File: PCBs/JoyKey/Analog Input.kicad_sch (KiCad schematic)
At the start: 2 parts, among them SW1 RotaryEncoder_Switch, U5 2_axis_analog_joystick_button

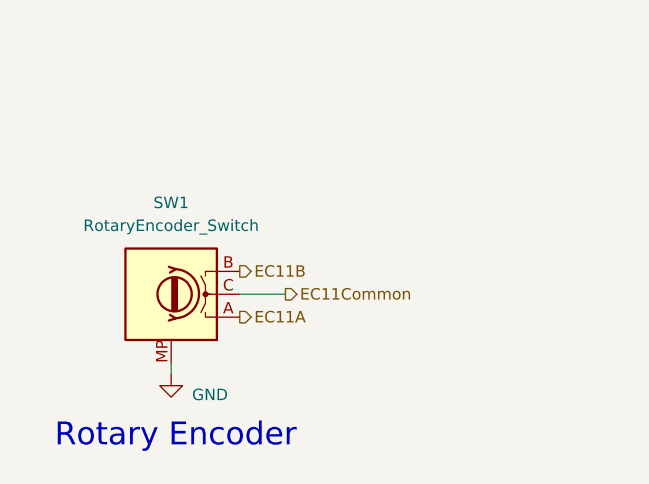
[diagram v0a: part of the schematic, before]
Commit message: Switched encoder to Alps SRBE110301 in sch
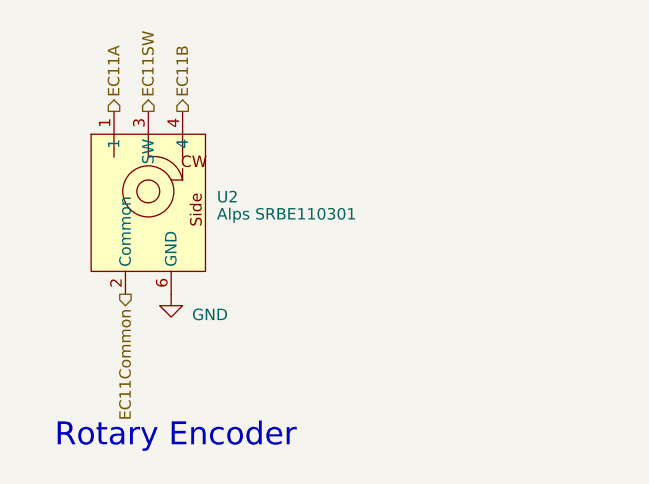
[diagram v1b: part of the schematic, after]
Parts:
- removed SW1: RotaryEncoder_Switch, Rotary_Encoder:RotaryEncoder_Alps_EC12E_Vertical_H20mm, symbol Device:RotaryEncoder
- added U2: Alps SRBE110301, custom_Interface_HID:Alps SRBE110301, symbol custom_Interface_HID:Alps_SRBE110301
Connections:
- net EC11A: now also U2.1
- net EC11B: now also U2.4
- net EC11Common: now also U2.2 (Common)
- net GND: now also U2.5 (GND), U2.6 (GND)
- new net EC11SW: U2.3 (SW)
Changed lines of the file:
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@@
 	(wire
 		(pts
-			(xy 127 87.63) (xy 121.92 87.63)
+			(xy 184.15 72.39) (xy 184.15 80.01)
 		)
 		(stroke
@@
 		)
 	)
-	(wire
-		(pts
-			(xy 184.15 72.39) (xy 184.15 80.01)
-		)
-		(stroke
-			(width 0)
-			(type default)
-		)
-	)
-	(wire
-		(pts
-			(xy 114.3 96.52) (xy 114.3 95.25)
-		)
-		(stroke
-			(width 0)
-			(type default)
-		)
-	)
 	(hierarchical_label "StickButtonB"
 		(shape output)
@@
 	(hierarchical_label "EC11A"
 		(shape output)
-		(at 121.92 90.17 0)
+		(at 107.95 67.31 90)
+		(effects
+			(font
+				(size 1.27 1.27)
+			)
+			(justify left)
+		)
+	)
+	(hierarchical_label "EC11SW"
+		(shape output)
+		(at 111.76 67.31 90)
 		(effects
 			(font
@@
 	(hierarchical_label "EC11B"
 		(shape output)
-		(at 121.92 85.09 0)
+		(at 115.57 67.31 90)
 		(effects
 			(font
@@
 	(hierarchical_label "EC11Common"
 		(shape output)
-		(at 127 87.63 0)
-		(effects
-			(font
-				(size 1.27 1.27)
-			)
-			(justify left)
+		(at 109.22 87.63 270)
+		(effects
+			(font
+				(size 1.27 1.27)
+			)
+			(justify right)
 		)
 	)
@@
 	)
 	(symbol
-		(lib_id "Device:RotaryEncoder")
-		(at 114.3 87.63 180)
+		(lib_id "custom_Interface_HID:Alps_SRBE110301")
+		(at 111.76 76.2 0)
 		(unit 1)
 		(exclude_from_sim no)
@@
 		(dnp no)
 		(fields_autoplaced yes)
-		(property "Reference" "SW1"
-			(at 114.3 77.47 0)
-			(effects
-				(font
-					(size 1.27 1.27)
-				)
-			)
-		)
-		(property "Value" "RotaryEncoder_Switch"
-			(at 114.3 80.01 0)
-			(effects
-				(font
-					(size 1.27 1.27)
-				)
-			)
-		)
-		(property "Footprint" "Rotary_Encoder:RotaryEncoder_Alps_EC12E_Vertical_H20mm"
-			(at 118.11 91.694 0)
-			(effects
-				(font
-					(size 1.27 1.27)
-				)
-				(hide yes)
-			)
-		)
-		(property "Datasheet" "~"
-			(at 114.3 94.234 0)
-			(effects
-				(font
-					(size 1.27 1.27)
-				)
-				(hide yes)
-			)
-		)
-		(property "Description" "Rotary encoder, dual channel, incremental quadrate outputs"
-			(at 114.3 87.63 0)
-			(effects
-				(font
-					(size 1.27 1.27)
-				)
-				(hide yes)
-			)
-		)
-		(pin "A"
-		)
-		(pin "B"
-		)
-		(pin "C"
-		)
-		(pin "MP"
+		(property "Reference" "U2"
+			(at 119.38 76.8349 0)
+			(effects
+				(font
+					(size 1.27 1.27)
+				)
+				(justify left)
+			)
+		)
+		(property "Value" "Alps SRBE110301"
+			(at 119.38 78.74 0)
+			(effects
+				(font
+					(size 1.27 1.27)
+				)
+				(justify left)
+			)
+		)
+		(property "Footprint" "custom_Interface_HID:Alps SRBE110301"
+			(at 111.76 76.2 0)
+			(effects
+				(font
+					(size 1.27 1.27)
+				)
+				(hide yes)
+			)
+		)
+		(property "Datasheet" ""
+			(at 111.76 76.2 0)
+			(effects
+				(font
+					(size 1.27 1.27)
+				)
+				(hide yes)
+			)
+		)
+		(property "Description" ""
+			(at 111.76 76.2 0)
+			(effects
+				(font
+					(size 1.27 1.27)
+				)
+				(hide yes)
+			)
+		)
+		(pin "5"
+		)
+		(pin "3"
+		)
+		(pin "6"
+		)
+		(pin "4"
+		)
+		(pin "2"
+		)
+		(pin "1"
 		)
 		(instances
 			(project "JoyKey"
 				(path "/7995ec7a-c14b-437e-b354-3eb74052b7cb/a78c392f-6f7c-48a6-aa3f-986a350bb68a"
-					(reference "SW1")
+					(reference "U2")
 					(unit 1)
 				)
@@
 	(symbol
 		(lib_id "power:GND")
-		(at 114.3 96.52 0)
+		(at 114.3 87.63 0)
 		(unit 1)
 		(exclude_from_sim no)
@@
 		(dnp no)
 		(property "Reference" "#PWR012"
-			(at 114.3 102.87 0)
+			(at 114.3 93.98 0)
 			(effects
 				(font
@@
 		)
 		(property "Value" "GND"
-			(at 118.618 98.806 0)
+			(at 118.618 89.916 0)
 			(effects
 				(font
@@
 		)
 		(property "Footprint" ""
-			(at 114.3 96.52 0)
-			(effects
-				(font
-					(size 1.27 1.27)
-				)
-				(hide yes)
-			)
-		)
-		(property "Datasheet" ""
-			(at 114.3 96.52 0)
+			(at 114.3 87.63 0)
+			(effects
+				(font
+					(size 1.27 1.27)
+				)
+				(hide yes)
+			)
+		)
+		(property "Datasheet" ""
+			(at 114.3 87.63 0)
 			(effects
 				(font
@@
 		)
 		(property "Description" "Power symbol creates a global label with name \"GND\" , ground"
-			(at 114.3 96.52 0)
-			(effects
-				(font
+			(at 114.3 87.63 0)
+			(effects
+				(font

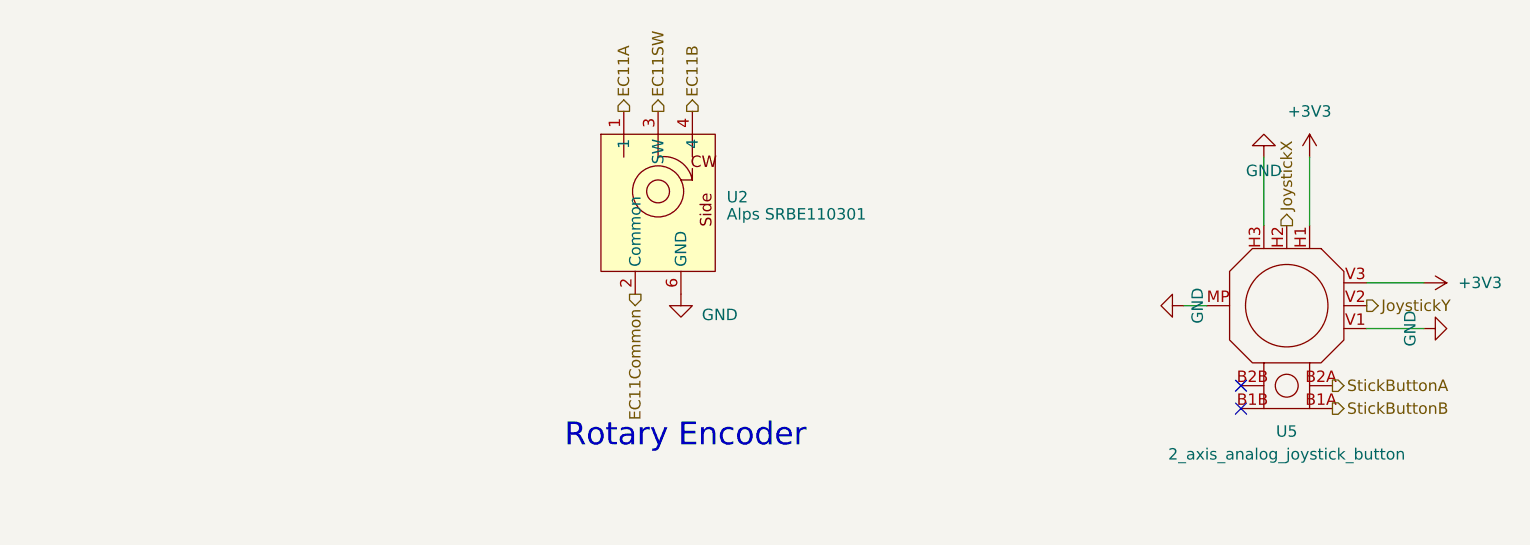
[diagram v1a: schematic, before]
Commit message: Add reverse mount for side encoder to simplifiy assembly
Now, if you want, you can get ALL SMD components on one side! I still prefer the encoder to be put on the top side because it is more central to the whole body, but of course, 2 sided assembly has its costs and I wanted to minimize that.
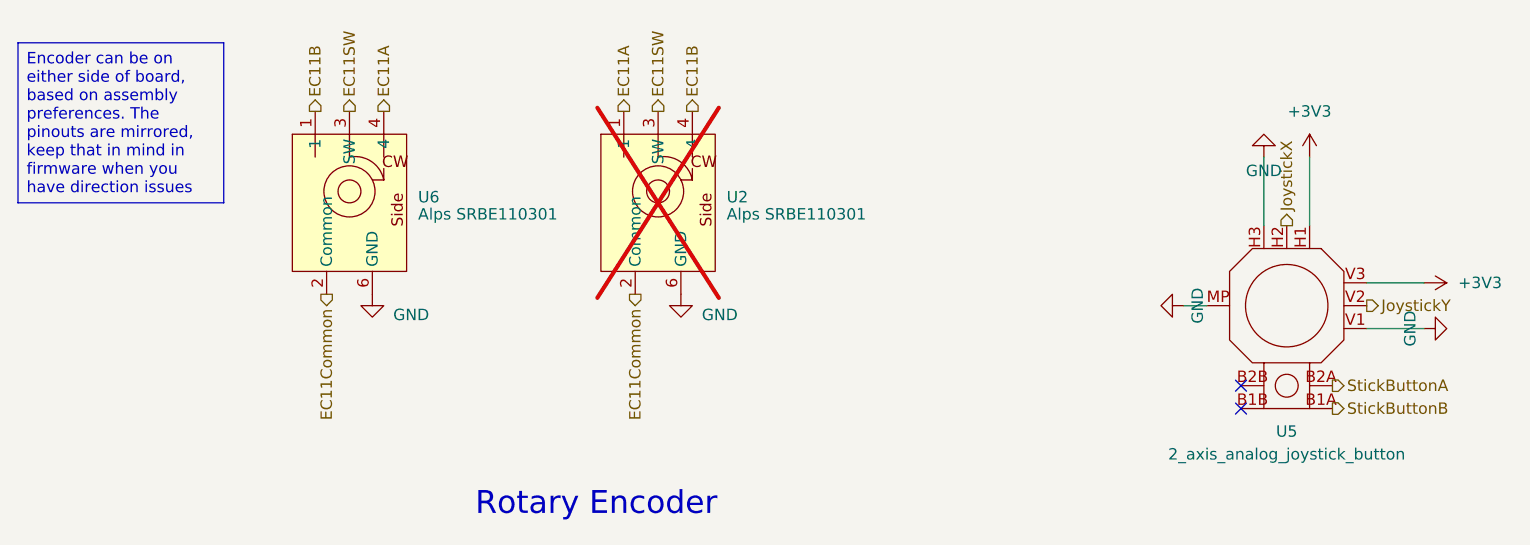
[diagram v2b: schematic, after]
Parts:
- added U6: Alps SRBE110301, custom_Interface_HID:Alps SRBE110301, symbol custom_Interface_HID:Alps_SRBE110301
- U2: now not fitted; now left out of the parts list
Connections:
- net EC11A: now also U6.4
- net EC11B: now also U6.1
- net EC11Common: now also U6.2 (Common)
- net EC11SW: now also U6.3 (SW)
- net GND: now also U6.5 (GND), U6.6 (GND)
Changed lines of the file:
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@@
 	(text "Rotary Encoder"
 		(exclude_from_sim no)
-		(at 114.808 103.378 0)
+		(at 104.902 110.998 0)
 		(effects
 			(font
 				(size 2.54 2.54)
 			)
+		)
+	)
+	(text_box "Encoder can be on either side of board, based on assembly preferences. The pinouts are mirrored, keep that in mind in firmware when you have direction issues"
+		(exclude_from_sim no)
+		(at 40.64 59.69 0)
+		(size 22.86 17.78)
+		(margins 0.9525 0.9525 0.9525 0.9525)
+		(stroke
+			(width 0)
+			(type solid)
+		)
+		(fill
+			(type none)
+		)
+		(effects
+			(font
+				(size 1.27 1.27)
+			)
+			(justify left top)
 		)
 	)
@@
 		)
 	)
+	(hierarchical_label "EC11B"
+		(shape output)
+		(at 73.66 67.31 90)
+		(effects
+			(font
+				(size 1.27 1.27)
+			)
+			(justify left)
+		)
+	)
 	(hierarchical_label "JoystickY"
 		(shape output)
@@
 		)
 	)
+	(hierarchical_label "EC11Common"
+		(shape output)
+		(at 74.93 87.63 270)
+		(effects
+			(font
+				(size 1.27 1.27)
+			)
+			(justify right)
+		)
+	)
 	(hierarchical_label "EC11A"
 		(shape output)
+		(at 81.28 67.31 90)
+		(effects
+			(font
+				(size 1.27 1.27)
+			)
+			(justify left)
+		)
+	)
+	(hierarchical_label "EC11A"
+		(shape output)
 		(at 107.95 67.31 90)
 		(effects
@@
 			)
 			(justify right)
+		)
+	)
+	(hierarchical_label "EC11SW"
+		(shape output)
+		(at 77.47 67.31 90)
+		(effects
+			(font
+				(size 1.27 1.27)
+			)
+			(justify left)
 		)
 	)
@@
 		(unit 1)
 		(exclude_from_sim no)
-		(in_bom yes)
-		(on_board yes)
-		(dnp no)
+		(in_bom no)
+		(on_board yes)
+		(dnp yes)
 		(fields_autoplaced yes)
 		(property "Reference" "U2"
@@
 	(symbol
 		(lib_id "power:GND")
+		(at 80.01 87.63 0)
+		(unit 1)
+		(exclude_from_sim no)
+		(in_bom yes)
+		(on_board yes)
+		(dnp no)
+		(property "Reference" "#PWR031"
+			(at 80.01 93.98 0)
+			(effects
+				(font
+					(size 1.27 1.27)
+				)
+				(hide yes)
+			)
+		)
+		(property "Value" "GND"
+			(at 84.328 89.916 0)
+			(effects
+				(font
+					(size 1.27 1.27)
+				)
+			)
+		)
+		(property "Footprint" ""
+			(at 80.01 87.63 0)
+			(effects
+				(font
+					(size 1.27 1.27)
+				)
+				(hide yes)
+			)
+		)
+		(property "Datasheet" ""
+			(at 80.01 87.63 0)
+			(effects
+				(font
+					(size 1.27 1.27)
+				)
+				(hide yes)
+			)
+		)
+		(property "Description" "Power symbol creates a global label with name \"GND\" , ground"
+			(at 80.01 87.63 0)
+			(effects
+				(font
+					(size 1.27 1.27)
+				)
+				(hide yes)
+			)
+		)
+		(pin "1"
+		)
+		(instances
+			(project "JoyKey"
+				(path "/7995ec7a-c14b-437e-b354-3eb74052b7cb/a78c392f-6f7c-48a6-aa3f-986a350bb68a"
+					(reference "#PWR031")
+					(unit 1)
+				)
+			)
+		)
+	)
+	(symbol
+		(lib_id "power:GND")
 		(at 179.07 72.39 180)
 		(unit 1)
@@
 					(unit 1)
 				)
+			)
+		)
+	)
+	(symbol
+		(lib_id "custom_Interface_HID:Alps_SRBE110301")
+		(at 77.47 76.2 0)
+		(unit 1)
+		(exclude_from_sim no)
+		(in_bom yes)
+		(on_board yes)
+		(dnp no)
+		(fields_autoplaced yes)
+		(property "Reference" "U6"
+			(at 85.09 76.8349 0)
+			(effects
+				(font
+					(size 1.27 1.27)
+				)
+				(justify left)
+			)
+		)
+		(property "Value" "Alps SRBE110301"
+			(at 85.09 78.74 0)
+			(effects
+				(font
+					(size 1.27 1.27)
+				)
+				(justify left)
+			)
+		)
+		(property "Footprint" "custom_Interface_HID:Alps SRBE110301"
+			(at 77.47 76.2 0)
+			(effects
+				(font
+					(size 1.27 1.27)
+				)
+				(hide yes)
+			)
+		)
+		(property "Datasheet" ""
+			(at 77.47 76.2 0)
+			(effects
+				(font
+					(size 1.27 1.27)
+				)
+				(hide yes)
+			)
+		)
+		(property "Description" ""
+			(at 77.47 76.2 0)
+			(effects
+				(font
+					(size 1.27 1.27)
+				)
+				(hide yes)
+			)
+		)
+		(pin "5"
+		)
+		(pin "3"
+		)
+		(pin "6"
+		)
+		(pin "4"
+		)
+		(pin "2"
+		)
+		(pin "1"
+		)
+		(instances
+			(project "JoyKey"
+				(path "/7995ec7a-c14b-437e-b354-3eb74052b7cb/a78c392f-6f7c-48a6-aa3f-986a350bb68a"
+					(reference "U6")
+					(unit 1)
+				)
